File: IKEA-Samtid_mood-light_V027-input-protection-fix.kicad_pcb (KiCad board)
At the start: 2 copper layers, 35.7 x 15.2 mm, 9 parts, among them P1 POWER, P2 CONN_1, P3 CONN_1, Q1 IRLML6401PbF, Q2 IRLML6401PbF

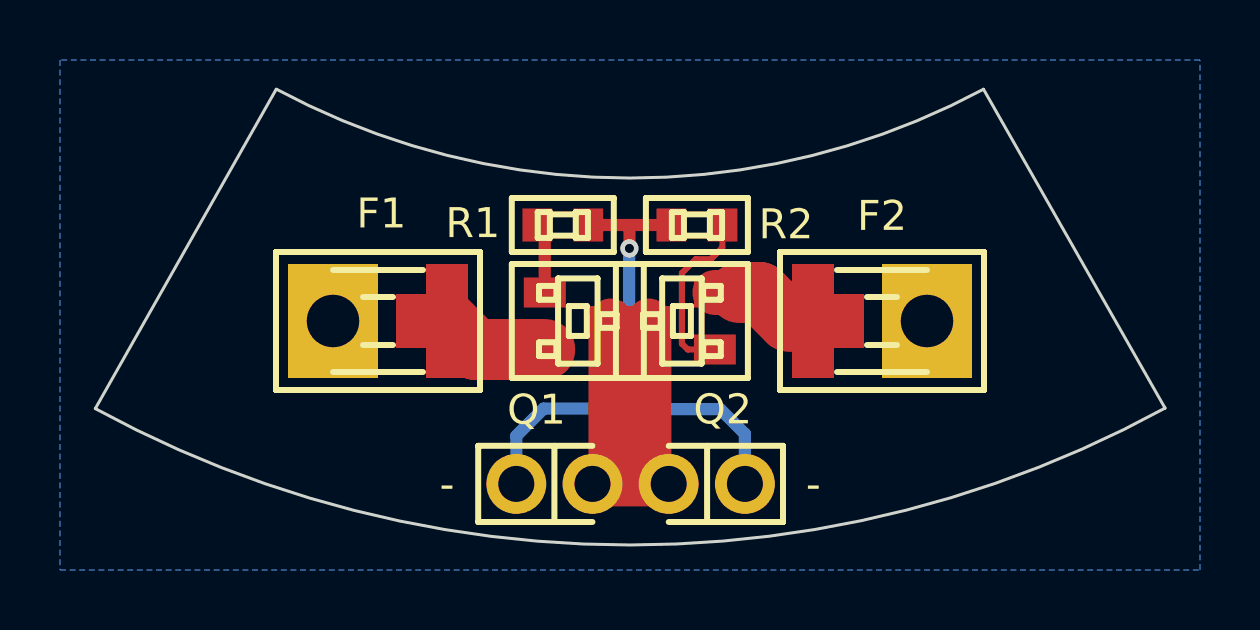
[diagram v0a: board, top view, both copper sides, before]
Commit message: One 3A poly-switch is enough: input-protection upgrade board for V0.27 boards.
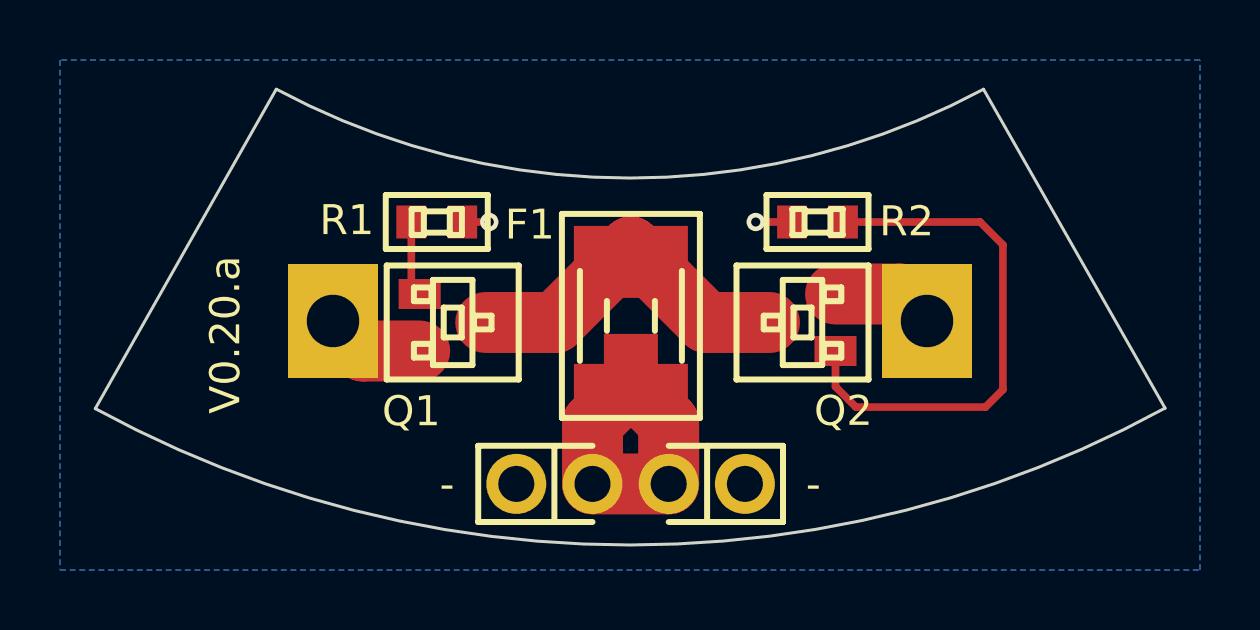
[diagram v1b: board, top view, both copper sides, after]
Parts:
- removed F2: 3A-poly, SM1812_1206-dual
- moved F1 8.43 mm to (150.0, 124.5), turned to 270 degrees
- moved R1 4.20 mm to (143.6, 121.4)
- moved Q1 4.17 mm to (144.1, 124.8)
- moved R2 4.02 mm to (156.2, 121.4)
- moved Q2 4.02 mm to (155.8, 124.8)
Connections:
- P1 pad 2: Net-(P1-Pad2) -> Net-(F1-Pad2)
- P1 pad 3: Net-(P1-Pad2) -> Net-(F1-Pad2)
- P2 pad 1: Net-(F1-Pad2) -> Net-(P2-Pad1)
- P3 pad 1: Net-(F2-Pad2) -> Net-(P3-Pad1)
- Q1 pad 2: Net-(F1-Pad1) -> Net-(P2-Pad1)
- Q1 pad 3: Net-(P1-Pad2) -> Net-(F1-Pad1)
- Q2 pad 2: Net-(F2-Pad1) -> Net-(P3-Pad1)
- Q2 pad 3: Net-(P1-Pad2) -> Net-(F1-Pad1)
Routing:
- net GND: track 20.3 -> 2.11 mm, vias 1 -> 2
- net Net-(P1-Pad2): track 13.9 -> 0.00 mm
- net Net-(Q2-Pad1): track 5.99 -> 17.8 mm
- net Net-(F1-Pad2): track 0.00 -> 10.2 mm
- net Net-(F1-Pad1): track 3.65 -> 11.5 mm
- net Net-(F2-Pad1): track 3.66 -> 0.00 mm
- net Net-(P3-Pad1): track 0.00 -> 3.42 mm
- net Net-(P2-Pad1): track 0.00 -> 3.30 mm
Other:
- board text added: "V0.20.a"
